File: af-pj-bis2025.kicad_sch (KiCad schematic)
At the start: 81 parts, among them J1 CN7, J2 CN10, J3 Conn_01x06, J4 Conn_Coaxial, J5 Barrel_Jack_MountingPin, J7 Conn_Coaxial, U1 MIC5237-5.0YU, U2 ALD114904APAL, U3 OPA2380AIDGKR, U4 THS4552IPWR, U5 REF5050IDR, U6 LT1991ACMS-TRPBF, U7 UA78L06ACPK, U8 ADS1220IPW

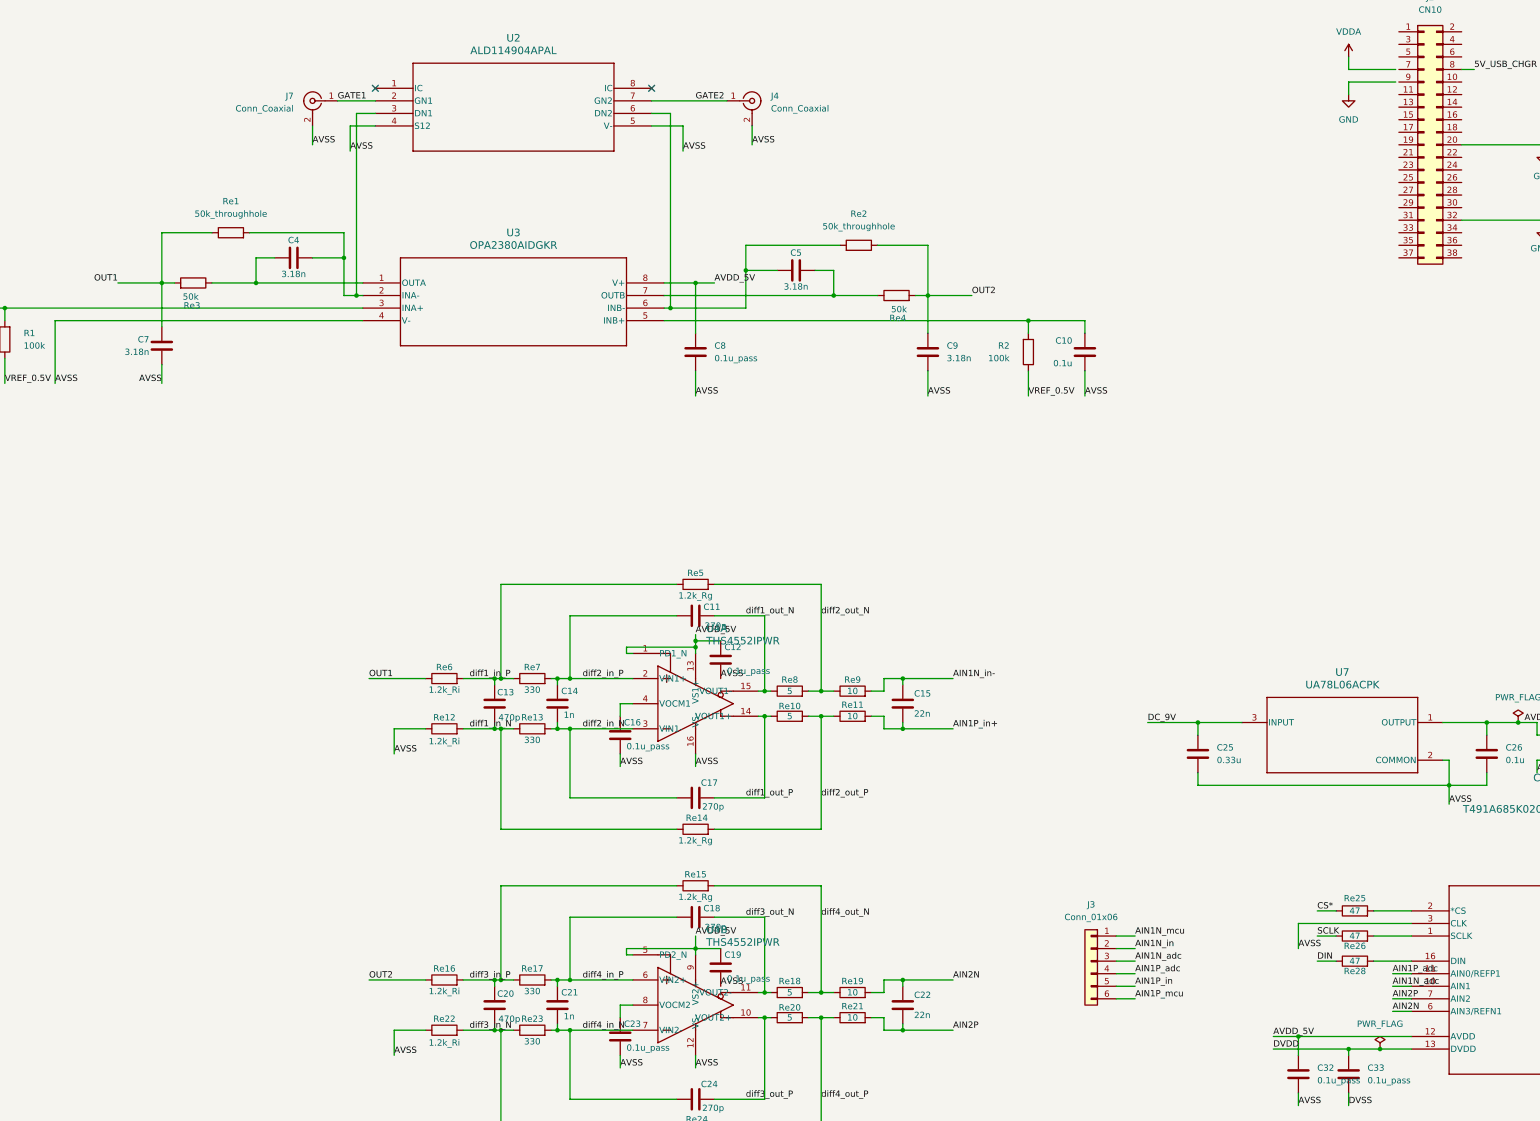
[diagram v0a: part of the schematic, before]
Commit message: AVSS接続完了
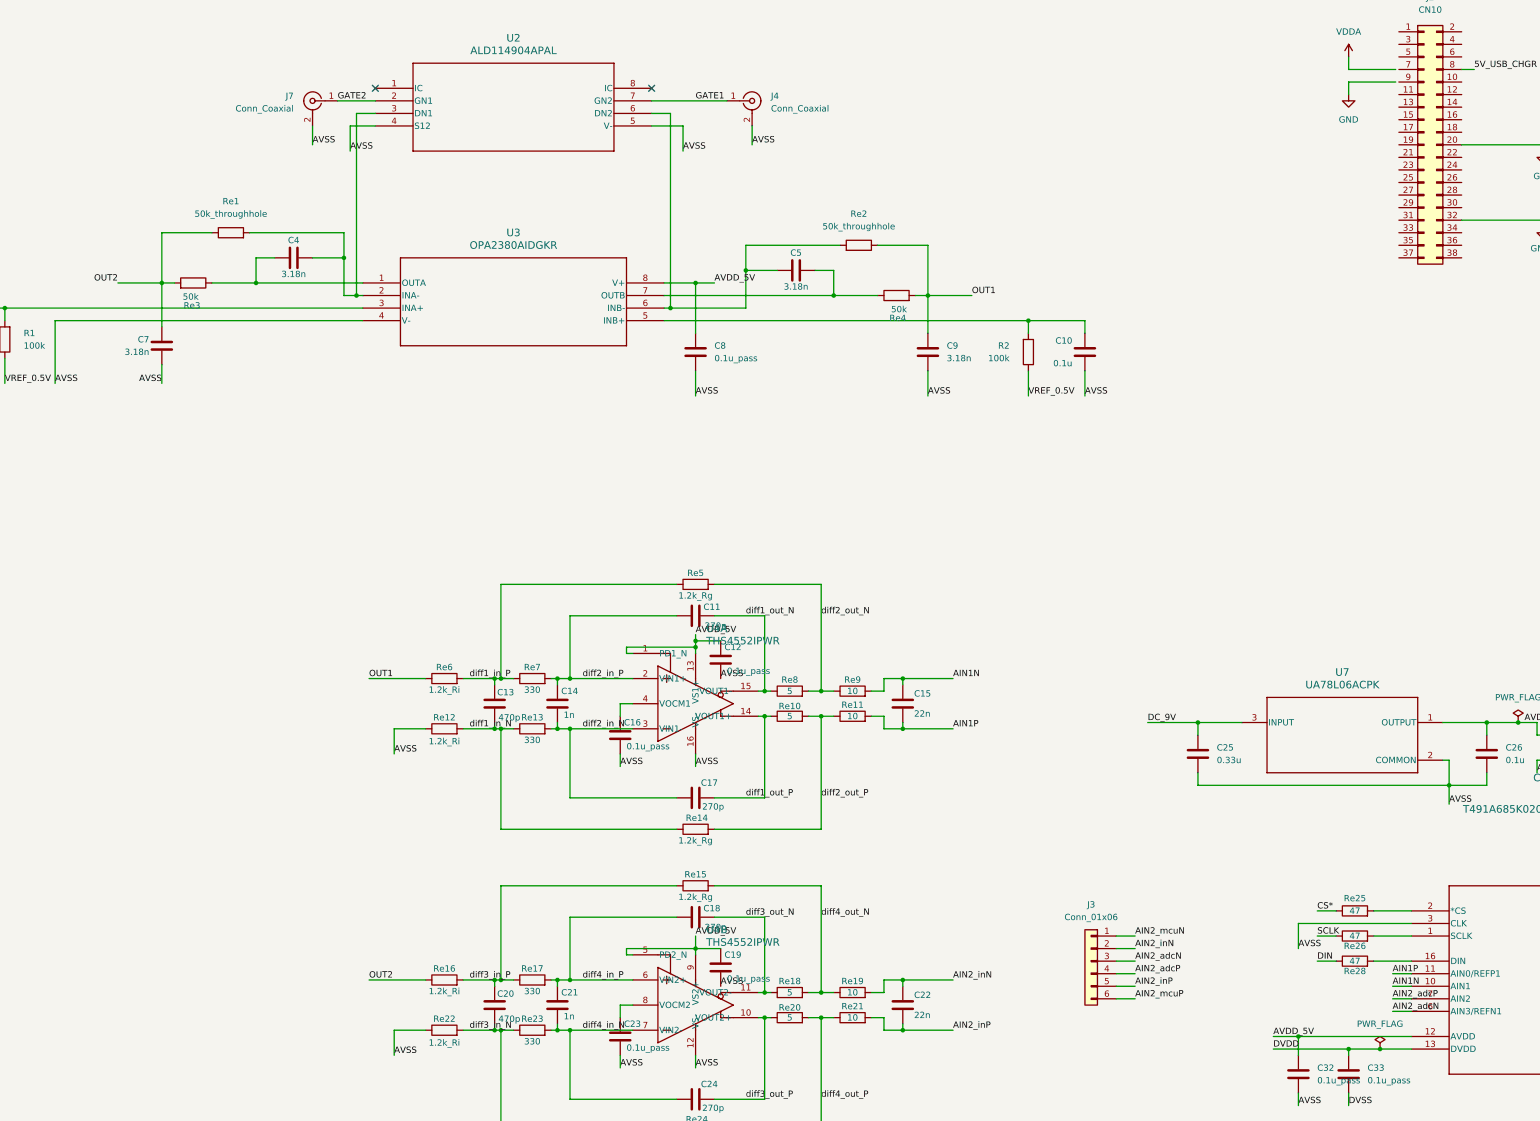
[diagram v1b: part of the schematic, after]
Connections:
- net AIN1N_in- is gone; now on net AIN1N: C15.2, Re9.2
- net AIN1P_in+ is gone; now on net AIN1P: C15.1, Re11.2
- net GATE1: now also J4.1 (In), U2.7 (GN2); no longer J7.1 (In), U2.2 (GN1)
- net GATE2: now also J7.1 (In), U2.2 (GN1); no longer J4.1 (In), U2.7 (GN2)
- net OUT1: now also C9.2, Re2.1, Re4.2; no longer C7.2, Re1.1, Re3.2
- net OUT2: now also C7.2, Re1.1, Re3.2; no longer C9.2, Re2.1, Re4.2
- net AIN1N_adc renamed AIN1N
- net AIN1N: no longer J3.3 (Pin_3)
- net AIN1N_in renamed AIN2_inN
- net AIN2_inN: now also C22.2, Re19.2
- net AIN1N_mcu renamed AIN2_mcuN
- net AIN1P_adc renamed AIN1P
- net AIN1P: no longer J3.4 (Pin_4)
- net AIN1P_in renamed AIN2_inP
- net AIN2_inP: now also C22.1, Re21.2
- net AIN1P_mcu renamed AIN2_mcuP
- removed net AIN2N: C22.2, Re19.2, U8.6 (AIN3/REFN1)
- removed net AIN2P: C22.1, Re21.2, U8.7 (AIN2)
- new net AIN2_adcN: J3.3 (Pin_3), U8.6 (AIN3/REFN1)
- new net AIN2_adcP: J3.4 (Pin_4), U8.7 (AIN2)
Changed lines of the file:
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@@
 		)
 	)
-	(label "AIN2N"
+	(label "AIN2_inN"
 		(at 226.06 314.96 0)
 		(effects
@@
 		)
 	)
-	(label "AIN2N"
+	(label "AIN2_adcN"
 		(at 314.96 321.31 0)
 		(effects
@@
 		)
 	)
-	(label "AIN2P"
+	(label "AIN2_inP"
 		(at 226.06 325.12 0)
 		(effects
@@
 		)
 	)
-	(label "OUT2"
+	(label "OUT1"
 		(at 229.87 176.53 0)
 		(effects
@@
 		)
 	)
-	(label "AIN1N_in-"
+	(label "AIN1N"
 		(at 226.06 254 0)
 		(effects
@@
 		)
 	)
-	(label "AIN1P_in+"
+	(label "AIN1P"
 		(at 226.06 264.16 0)
 		(effects
@@
 		)
 	)
-	(label "AIN1N_in"
+	(label "AIN2_inN"
 		(at 262.89 308.61 0)
 		(effects
@@
 		)
 	)
-	(label "AIN1N_adc"
+	(label "AIN1N"
 		(at 314.96 316.23 0)
 		(effects
@@
 		)
 	)
-	(label "AIN1N_mcu"
+	(label "AIN2_mcuN"
 		(at 262.89 306.07 0)
 		(effects
@@
 		)
 	)
-	(label "AIN1P_adc"
+	(label "AIN1P"
 		(at 314.96 313.69 0)
 		(effects
@@
 		)
 	)
-	(label "AIN1P_mcu"
+	(label "AIN2_mcuP"
 		(at 262.89 318.77 0)
 		(effects
@@
 		)
 	)
-	(label "GATE1"
+	(label "GATE2"
 		(at 101.6 137.16 0)
 		(effects
@@
 		)
 	)
-	(label "AIN1P_in"
+	(label "AIN2_inP"
 		(at 262.89 316.23 0)
 		(effects
@@
 		)
 	)
-	(label "AIN1N_adc"
+	(label "AIN2_adcN"
 		(at 262.89 311.15 0)
 		(effects
@@
 		)
 	)
-	(label "AIN2P"
+	(label "AIN2_adcP"
 		(at 314.96 318.77 0)
 		(effects
@@
 		)
 	)
-	(label "GATE2"
+	(label "GATE1"
 		(at 173.99 137.16 0)
 		(effects
@@
 		)
 	)
-	(label "AIN1P_adc"
+	(label "AIN2_adcP"
 		(at 262.89 313.69 0)
 		(effects
@@
 		)
 	)
-	(label "OUT1"
+	(label "OUT2"
 		(at 57.15 173.99 180)
 		(effects

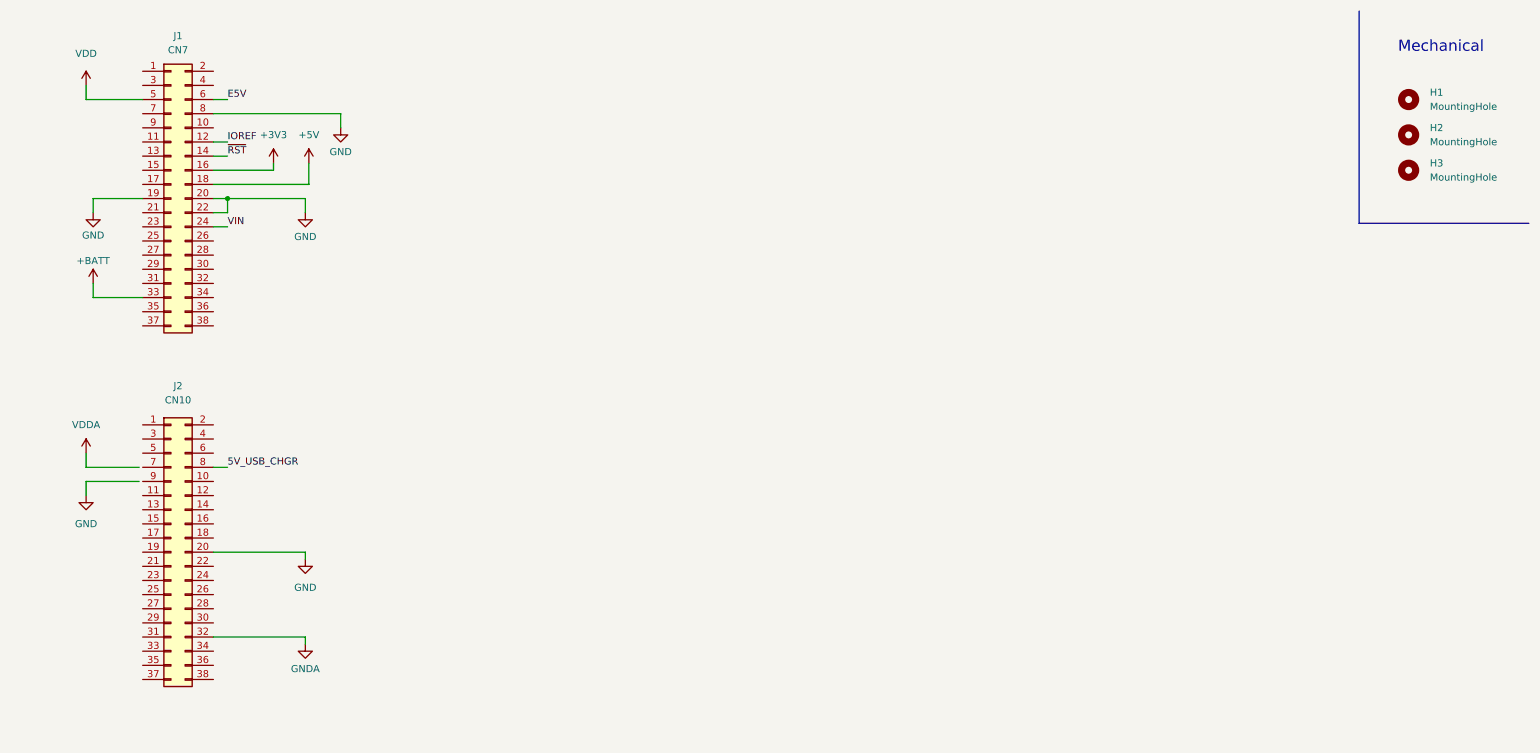
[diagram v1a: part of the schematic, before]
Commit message: LCDの配線完了
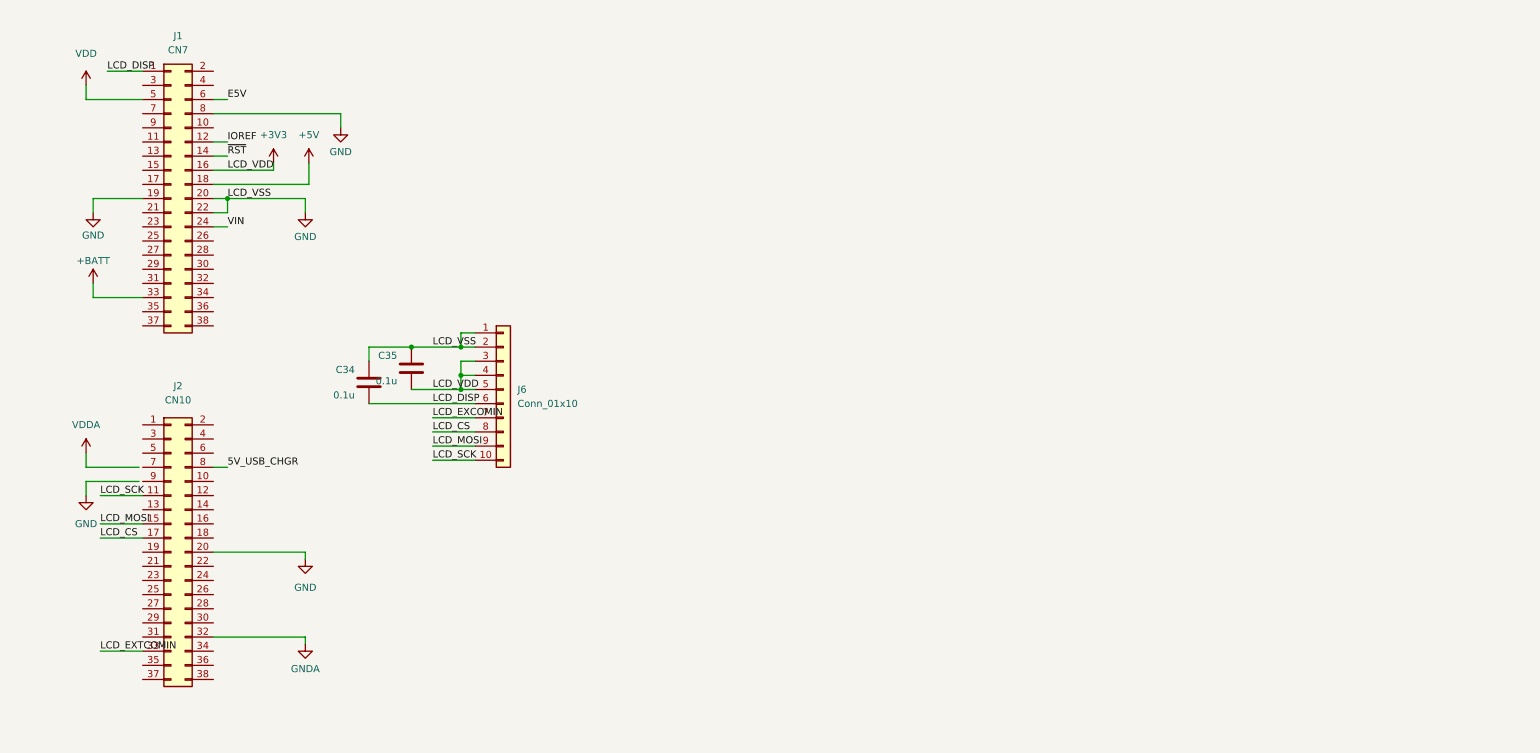
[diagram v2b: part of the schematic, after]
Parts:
- removed H1, H2, H3: MountingHole, MountingHole:MountingHole_3.2mm_M3, symbol Mechanical:MountingHole
- added C34, C35: 0.1u, Capacitor_SMD:C_0805_2012Metric_Pad1.18x1.45mm_HandSolder, symbol Device:C
- added J6: Conn_01x10, Connector_JST:JST_XH_B10B-XH-A_1x10_P2.50mm_Vertical, symbol Connector_Generic:Conn_01x10
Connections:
- net +3V3: now also C35.1, J6.3 (Pin_3), J6.4 (Pin_4), J6.5 (Pin_5)
- net GND: now also C34.2, C35.2, J6.1 (Pin_1), J6.2 (Pin_2)
- net LCD_DISP: now reaches J1.1 (Pin_1)
- net LCD_DISP: now also C34.1, J6.6 (Pin_6)
- net LCD_SCK: now reaches J2.11 (Pin_11)
- net LCD_SCK: now also J6.10 (Pin_10)
- net LCD_MOSI: now reaches J2.15 (Pin_15)
- net LCD_MOSI: now also J6.9 (Pin_9)
- net LCD_CS: now reaches J2.17 (Pin_17)
- net LCD_CS: now also J6.8 (Pin_8)
- net LCD_EXTCOMIN: now reaches J2.33 (Pin_33)
- new net LCD_EXCOMIN: J6.7 (Pin_7)
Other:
- note removed: "Mechanical"

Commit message: ADCのディジタル配線完了
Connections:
- net CS* is gone; now on net ADC_CS: Re25.1
- net DIN is gone; now on net ADC_MOSI: Re28.1
- net DOUT is gone; now on net ADC_MISO: Re27.2
- net DRDY is gone; now on net ADC_DRDY: Re29.2
- net SCLK is gone; now on net ADC_SCLK: Re26.1
- net ADC_MISO: now reaches J1.35 (Pin_35)
- net ADC_MOSI: now reaches J1.36 (Pin_36)
- net ADC_CS: now reaches J2.21 (Pin_21)
- net ADC_SCLK: now reaches J2.25 (Pin_25)
- net ADC_DRDY: now reaches J2.26 (Pin_26)
- net LCD_SCK renamed LCD_SCLK
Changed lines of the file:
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@@
 	(wire
 		(pts
+			(xy 307.34 102.87) (xy 316.23 102.87)
+		)
+		(stroke
+			(width 0)
+			(type default)
+		)
+	)
+	(wire
+		(pts
 			(xy 212.09 317.5) (xy 212.09 314.96)
 		)
@@
 	(wire
 		(pts
+			(xy 308.61 148.59) (xy 316.23 148.59)
+		)
+		(stroke
+			(width 0)
+			(type default)
+		)
+	)
+	(wire
+		(pts
 			(xy 161.29 309.88) (xy 160.02 309.88)
 		)
@@
 	(wire
 		(pts
+			(xy 328.93 153.67) (xy 337.82 153.67)
+		)
+		(stroke
+			(width 0)
+			(type default)
+		)
+	)
+	(wire
+		(pts
 			(xy 167.64 173.99) (xy 173.99 173.99)
 		)
@@
 	(wire
 		(pts
+			(xy 328.93 102.87) (xy 336.55 102.87)
+		)
+		(stroke
+			(width 0)
+			(type default)
+		)
+	)
+	(wire
+		(pts
 			(xy 146.05 254) (xy 148.59 254)
 		)
@@
 	(wire
 		(pts
+			(xy 308.61 153.67) (xy 316.23 153.67)
+		)
+		(stroke
+			(width 0)
+			(type default)
+		)
+	)
+	(wire
+		(pts
 			(xy 167.64 181.61) (xy 241.3 181.61)
 		)
@@
 		)
 	)
-	(label "SCLK"
+	(label "ADC_SCLK"
 		(at 299.72 306.07 0)
 		(effects
@@
 		)
 	)
-	(label "DIN"
+	(label "ADC_MOSI"
 		(at 299.72 311.15 0)
 		(effects
@@
 		)
 	)
-	(label "DOUT"
+	(label "ADC_MISO"
 		(at 421.64 308.61 0)
 		(effects
@@
 		)
 	)
+	(label "ADC_DRDY"
+		(at 337.82 153.67 0)
+		(effects
+			(font
+				(size 1.27 1.27)
+			)
+			(justify left bottom)
+		)
+	)
 	(label "AVSS"
 		(at 179.07 316.23 0)
@@
 		)
 	)
-	(label "LCD_SCK"
+	(label "LCD_SCLK"
 		(at 368.3 129.54 0)
 		(effects
@@
 		)
 	)
-	(label "LCD_SCK"
+	(label "LCD_SCLK"
 		(at 308.61 135.89 0)
 		(effects
@@
 		)
 	)
-	(label "CS*"
+	(label "ADC_CS"
 		(at 299.72 300.99 0)
 		(effects
@@
 		)
 	)
+	(label "ADC_SCLK"
+		(at 308.61 153.67 0)
+		(effects
+			(font
+				(size 1.27 1.27)
+			)
+			(justify left bottom)
+		)
+	)
 	(label "AVSS"
 		(at 173.99 332.74 0)
@@
 		)
 	)
+	(label "ADC_MOSI"
+		(at 336.55 102.87 0)
+		(effects
+			(font
+				(size 1.27 1.27)
+			)
+			(justify left bottom)
+		)
+	)
 	(label "VREF_0.5V"
 		(at 490.22 273.05 0)
@@
 		)
 	)
+	(label "ADC_MISO"
+		(at 307.34 102.87 0)
+		(effects
+			(font
+				(size 1.27 1.27)
+			)
+			(justify left bottom)
+		)
+	)
 	(label "AVSS"
 		(at 113.03 269.24 0)
@@
 		)
 	)
-	(label "DRDY"
+	(label "ADC_DRDY"
 		(at 421.64 311.15 0)
 		(effects
@@
 		)
 	)
+	(label "ADC_CS"
+		(at 308.61 148.59 0)
+		(effects
+			(font
+				(size 1.27 1.27)
+			)
+			(justify left bottom)
+		)
+	)
 	(label "AVSS"
 		(at 414.02 330.2 0)
@@
 		(on_board yes)
 		(dnp no)
-		(fields_autoplaced yes)
 		(property "Reference" "#PWR0105"
 			(at 345.44 153.67 0)
@@
 		)
 		(property "Value" "GND"
-			(at 345.44 152.4 0)
+			(at 347.218 150.622 0)
 			(effects
 				(font

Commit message: EdgeCutsを調整した
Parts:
- removed J6: Conn_01x10, Connector_JST:JST_XH_B10B-XH-A_1x10_P2.50mm_Vertical, symbol Connector_Generic:Conn_01x10
- added J8: Conn_01x10, Connector_JST:JST_XH_B10B-XH-A_1x10_P2.50mm_Vertical, symbol Connector_Generic:Conn_01x10
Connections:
- net DVDD is gone; now on net +3V3: C33.1, U8.13 (DVDD)
- net DVSS is gone; now on net AVSS: C33.2, U8.4 (DGND)
- net +3V3: now also J8.3 (Pin_3), J8.4 (Pin_4), J8.5 (Pin_5)
- net GND: now also J8.1 (Pin_1), J8.2 (Pin_2)
- net LCD_CS: now also J8.8 (Pin_8)
- net LCD_DISP: now also J8.6 (Pin_6)
- net LCD_EXCOMIN: now also J8.7 (Pin_7)
- net LCD_MOSI: now also J8.9 (Pin_9)
- net LCD_SCLK: now also J8.10 (Pin_10)
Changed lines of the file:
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@@
 	(wire
 		(pts
+			(xy 279.4 349.25) (xy 287.02 349.25)
+		)
+		(stroke
+			(width 0)
+			(type default)
+		)
+	)
+	(wire
+		(pts
 			(xy 483.87 262.89) (xy 486.41 262.89)
 		)
@@
 		)
 	)
-	(label "LCD_VDD"
+	(label "DVDD"
 		(at 368.3 116.84 0)
 		(effects
@@
 	)
 	(label "AVSS"
+		(at 287.02 349.25 0)
+		(effects
+			(font
+				(size 1.27 1.27)
+			)
+			(justify left bottom)
+		)
+	)
+	(label "AVSS"
 		(at 173.99 271.78 0)
 		(effects
@@
 		)
 	)
-	(label "LCD_VDD"
+	(label "DVDD"
 		(at 331.47 77.47 0)
 		(effects
@@
 		)
 	)
+	(label "DVSS"
+		(at 279.4 349.25 0)
+		(effects
+			(font
+				(size 1.27 1.27)
+			)
+			(justify left bottom)
+		)
+	)
 	(label "AVSS"
 		(at 96.52 146.05 0)
@@
 	)
 	(symbol
-		(lib_id "Connector_Generic:Conn_01x10")
-		(at 381 116.84 0)
-		(unit 1)
-		(exclude_from_sim no)
-		(in_bom yes)
-		(on_board yes)
-		(dnp no)
-		(fields_autoplaced yes)
-		(property "Reference" "J6"
-			(at 383.54 116.8399 0)
-			(effects
-				(font
-					(size 1.27 1.27)
-				)
-				(justify left)
-			)
-		)
-		(property "Value" "Conn_01x10"
-			(at 383.54 119.3799 0)
-			(effects
-				(font
-					(size 1.27 1.27)
-				)
-				(justify left)
-			)
-		)
-		(property "Footprint" "Connector_JST:JST_XH_B10B-XH-A_1x10_P2.50mm_Vertical"
-			(at 381 116.84 0)
-			(effects
-				(font
-					(size 1.27 1.27)
-				)
-				(hide yes)
-			)
-		)
-		(property "Datasheet" "~"
-			(at 381 116.84 0)
-			(effects
-				(font
-					(size 1.27 1.27)
-				)
-				(hide yes)
-			)
-		)
-		(property "Description" "Generic connector, single row, 01x10, script generated (kicad-library-utils/schlib/autogen/connector/)"
-			(at 381 116.84 0)
-			(effects
-				(font
-					(size 1.27 1.27)
-				)
-				(hide yes)
-			)
-		)
-		(pin "2"
-		)
-		(pin "4"
-		)
-		(pin "3"
-		)
-		(pin "6"
-		)
-		(pin "7"
-		)
-		(pin "5"
-		)
-		(pin "10"
-		)
-		(pin "1"
-		)
-		(pin "9"
-		)
-		(pin "8"
-		)
-		(instances
-			(project ""
-				(path "/0c43c024-04be-42a3-97bf-885833c3aea8"
-					(reference "J6")
-					(unit 1)
-				)
-			)
-		)
-	)
-	(symbol
 		(lib_id "power:VDDA")
 		(at 306.07 128.27 0)
@@
 					(unit 1)
 				)
+			)
+		)
+	)
+	(symbol
+		(lib_id "Connector_Generic:Conn_01x10")
+		(at 381 116.84 0)
+		(unit 1)
+		(exclude_from_sim no)
+		(in_bom yes)
+		(on_board yes)
+		(dnp no)
+		(fields_autoplaced yes)
+		(property "Reference" "J8"
+			(at 383.54 116.8399 0)
+			(effects
+				(font
+					(size 1.27 1.27)
+				)
+				(justify left)
+			)
+		)
+		(property "Value" "Conn_01x10"
+			(at 383.54 119.3799 0)
+			(effects
+				(font
+					(size 1.27 1.27)
+				)
+				(justify left)
+			)
+		)
+		(property "Footprint" "Connector_JST:JST_XH_B10B-XH-A_1x10_P2.50mm_Vertical"
+			(at 381 116.84 0)
+			(effects
+				(font
+					(size 1.27 1.27)
+				)
+				(hide yes)
+			)
+		)
+		(property "Datasheet" "~"
+			(at 381 116.84 0)
+			(effects
+				(font
+					(size 1.27 1.27)
+				)
+				(hide yes)
+			)
+		)
+		(property "Description" "Generic connector, single row, 01x10, script generated (kicad-library-utils/schlib/autogen/connector/)"
+			(at 381 116.84 0)
+			(effects
+				(font
+					(size 1.27 1.27)
+				)
+				(hide yes)
+			)
+		)
+		(pin "5"
+		)
+		(pin "6"
+		)
+		(pin "3"
+		)
+		(pin "10"
+		)
+		(pin "1"
+		)
+		(pin "2"
+		)
+		(pin "4"
+		)
+		(pin "7"
+		)
+		(pin "9"
+		)
+		(pin "8"
+		)
+		(instances
+			(project ""
+				(path "/0c43c024-04be-42a3-97bf-885833c3aea8"
+					(reference "J8")
+					(unit 1)
+				)
